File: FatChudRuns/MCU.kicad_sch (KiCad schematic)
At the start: 16 parts, among them SW1 SW_Push, SW2 SW_DIP_x01, U1 STM32F107RBTx

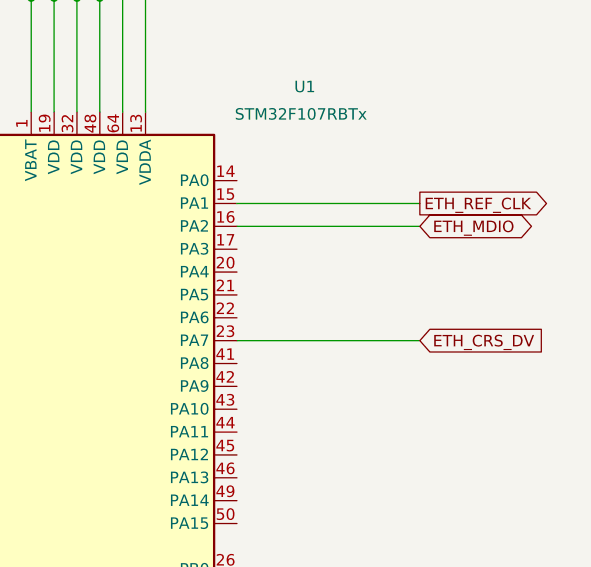
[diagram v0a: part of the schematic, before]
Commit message: connected phy to uC and added strapping options
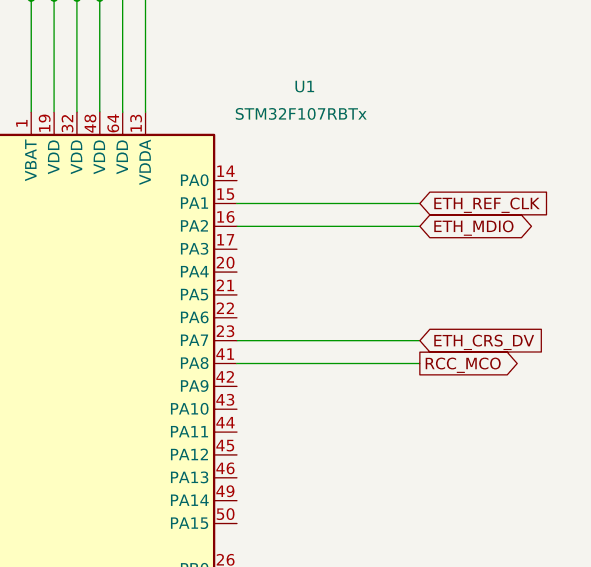
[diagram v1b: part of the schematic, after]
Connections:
- net RCC_MCO: now reaches U1.41 (PA8)
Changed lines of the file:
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@@
 	(generator "eeschema")
 	(generator_version "9.0")
-	(paper "A4")
+	(paper "A3")
 	(junction
 		(at 78.74 63.5)
@@
 		(pts
 			(xy 24.13 179.07) (xy 24.13 185.42)
+		)
+		(stroke
+			(width 0)
+			(type default)
+		)
+	)
+	(wire
+		(pts
+			(xy 170.18 78.74) (xy 190.5 78.74)
 		)
 		(stroke
@@
 		)
 	)
+	(global_label "RCC_MCO"
+		(shape output)
+		(at 190.5 78.74 0)
+		(fields_autoplaced yes)
+		(effects
+			(font
+				(size 1.27 1.27)
+			)
+			(justify left)
+		)
+		(property "Intersheetrefs" "${INTERSHEET_REFS}"
+			(at 202.4098 78.74 0)
+			(effects
+				(font
+					(size 1.27 1.27)
+				)
+				(justify left)
+				(hide yes)
+			)
+		)
+	)
 	(global_label "ETH_TXD0"
 		(shape output)
@@
 	)
 	(global_label "ETH_REF_CLK"
-		(shape output)
+		(shape input)
 		(at 190.5 60.96 0)
 		(fields_autoplaced yes)

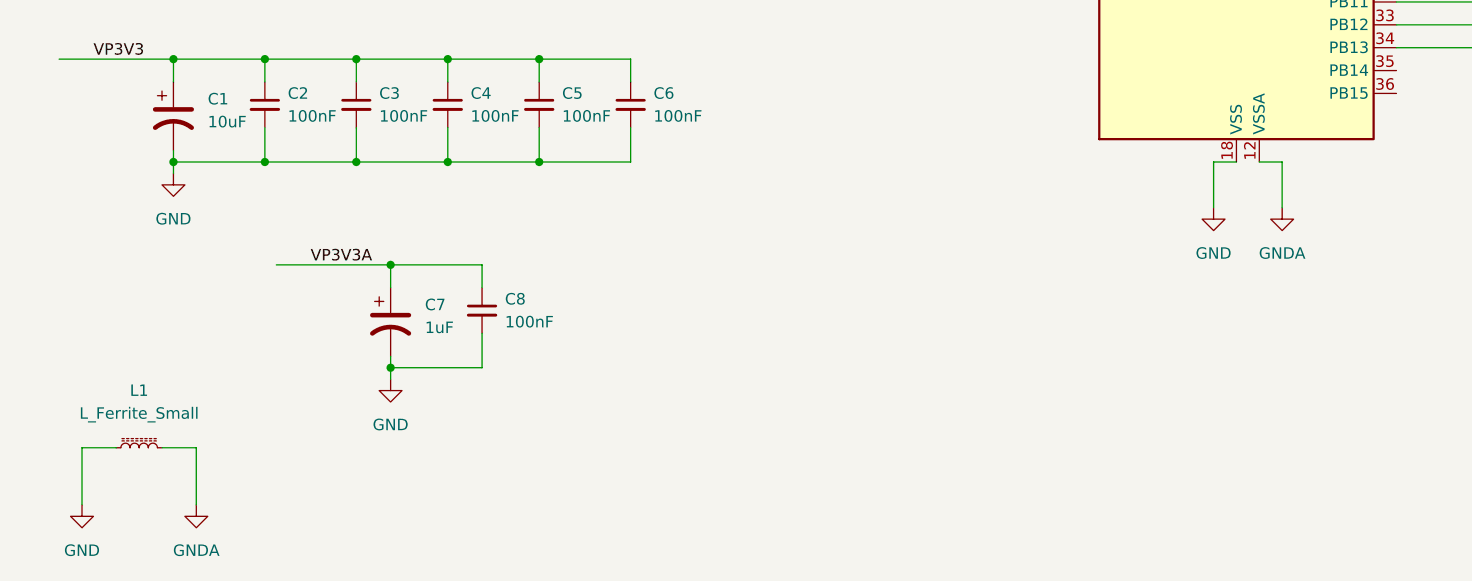
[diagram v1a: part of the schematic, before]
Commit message: selected rj45 w/ mag, fixed filtering for power, added snippets of layout recs
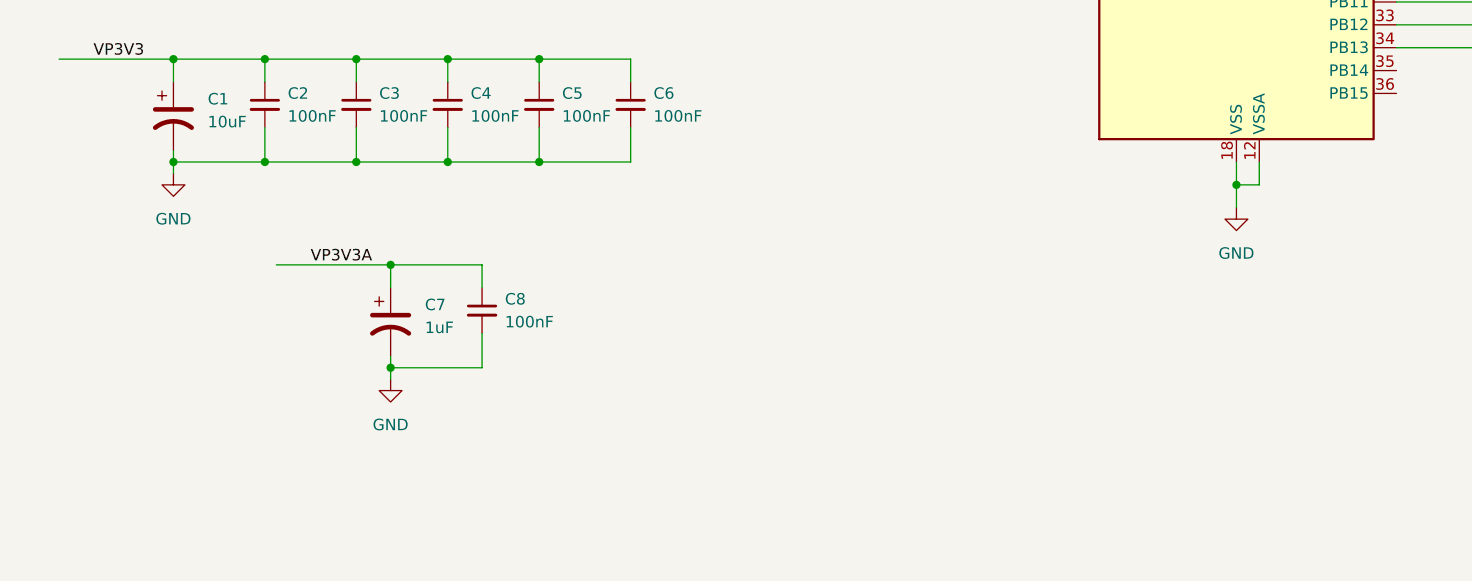
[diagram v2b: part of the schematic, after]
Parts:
- removed L1: L_Ferrite_Small, symbol Device:L_Ferrite_Small
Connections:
- net GNDA is gone; now on net GND: U1.12 (VSSA)

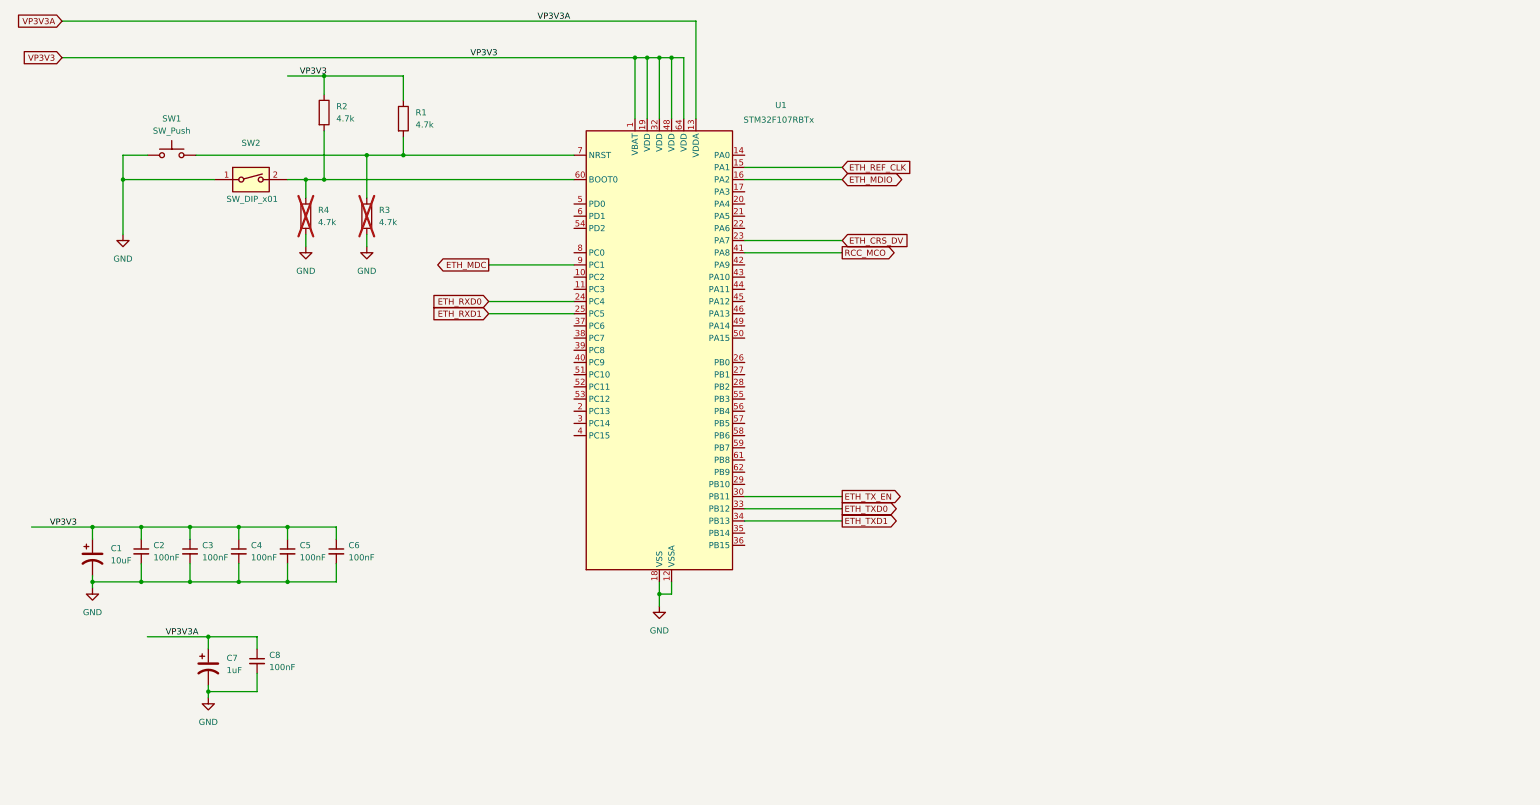
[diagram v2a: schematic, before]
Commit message: added connectors for gpio and jtag, need to verify orientation
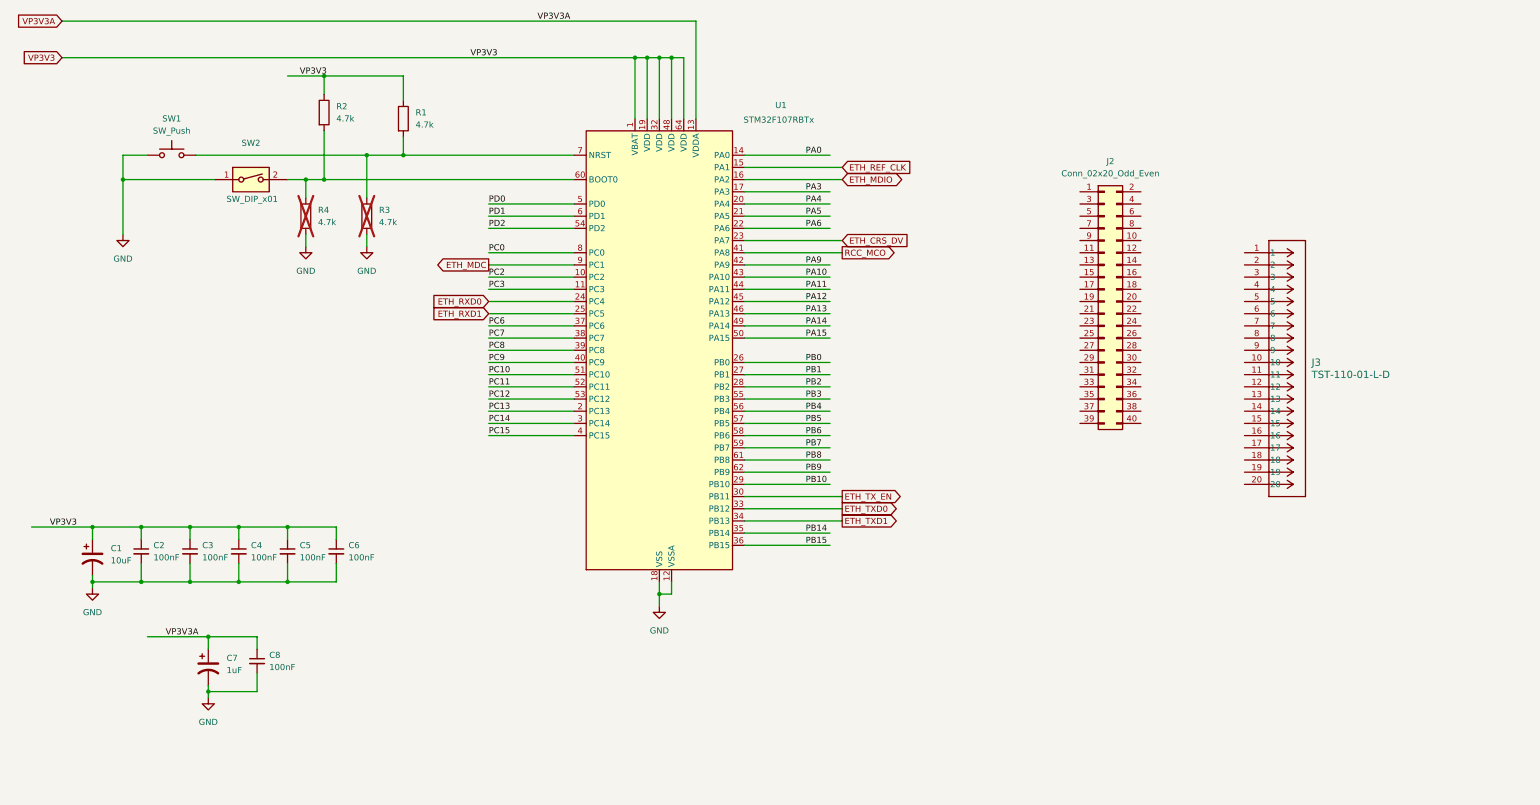
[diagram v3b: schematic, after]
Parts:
- added J2: Conn_02x20_Odd_Even, Connector_PinSocket_2.54mm:PinSocket_2x20_P2.54mm_Vertical, symbol Connector_Generic:Conn_02x20_Odd_Even
- added J3: TST-110-01-L-D, JTAG_20p_2.54mm:CONN20_TST_33P02X9P27_SAI, symbol TST_110_01_L_D:TST-110-01-L-D
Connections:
- net PC2: now reaches U1.10 (PC2)
- net PC3: now reaches U1.11 (PC3)
- net PA0: now reaches U1.14 (PA0)
- net PA3: now reaches U1.17 (PA3)
- net PC13: now reaches U1.2 (PC13)
- net PA4: now reaches U1.20 (PA4)
- net PA5: now reaches U1.21 (PA5)
- net PA6: now reaches U1.22 (PA6)
- net PB0: now reaches U1.26 (PB0)
- net PB1: now reaches U1.27 (PB1)
- net PB2: now reaches U1.28 (PB2)
- net PB10: now reaches U1.29 (PB10)
- net PC14: now reaches U1.3 (PC14)
- net PB14: now reaches U1.35 (PB14)
- net PB15: now reaches U1.36 (PB15)
- net PC6: now reaches U1.37 (PC6)
- net PC7: now reaches U1.38 (PC7)
- net PC8: now reaches U1.39 (PC8)
- net PC15: now reaches U1.4 (PC15)
- net PC9: now reaches U1.40 (PC9)
- net PA9: now reaches U1.42 (PA9)
- net PA10: now reaches U1.43 (PA10)
- net PA11: now reaches U1.44 (PA11)
- net PA12: now reaches U1.45 (PA12)
- net PA13: now reaches U1.46 (PA13)
- net PA14: now reaches U1.49 (PA14)
- net PD0: now reaches U1.5 (PD0)
- net PA15: now reaches U1.50 (PA15)
- net PC10: now reaches U1.51 (PC10)
- net PC11: now reaches U1.52 (PC11)
- net PC12: now reaches U1.53 (PC12)
- net PD2: now reaches U1.54 (PD2)
- net PB3: now reaches U1.55 (PB3)
- net PB4: now reaches U1.56 (PB4)
- net PB5: now reaches U1.57 (PB5)
- net PB6: now reaches U1.58 (PB6)
- net PB7: now reaches U1.59 (PB7)
- net PD1: now reaches U1.6 (PD1)
- net PB8: now reaches U1.61 (PB8)
- net PB9: now reaches U1.62 (PB9)
- net PC0: now reaches U1.8 (PC0)

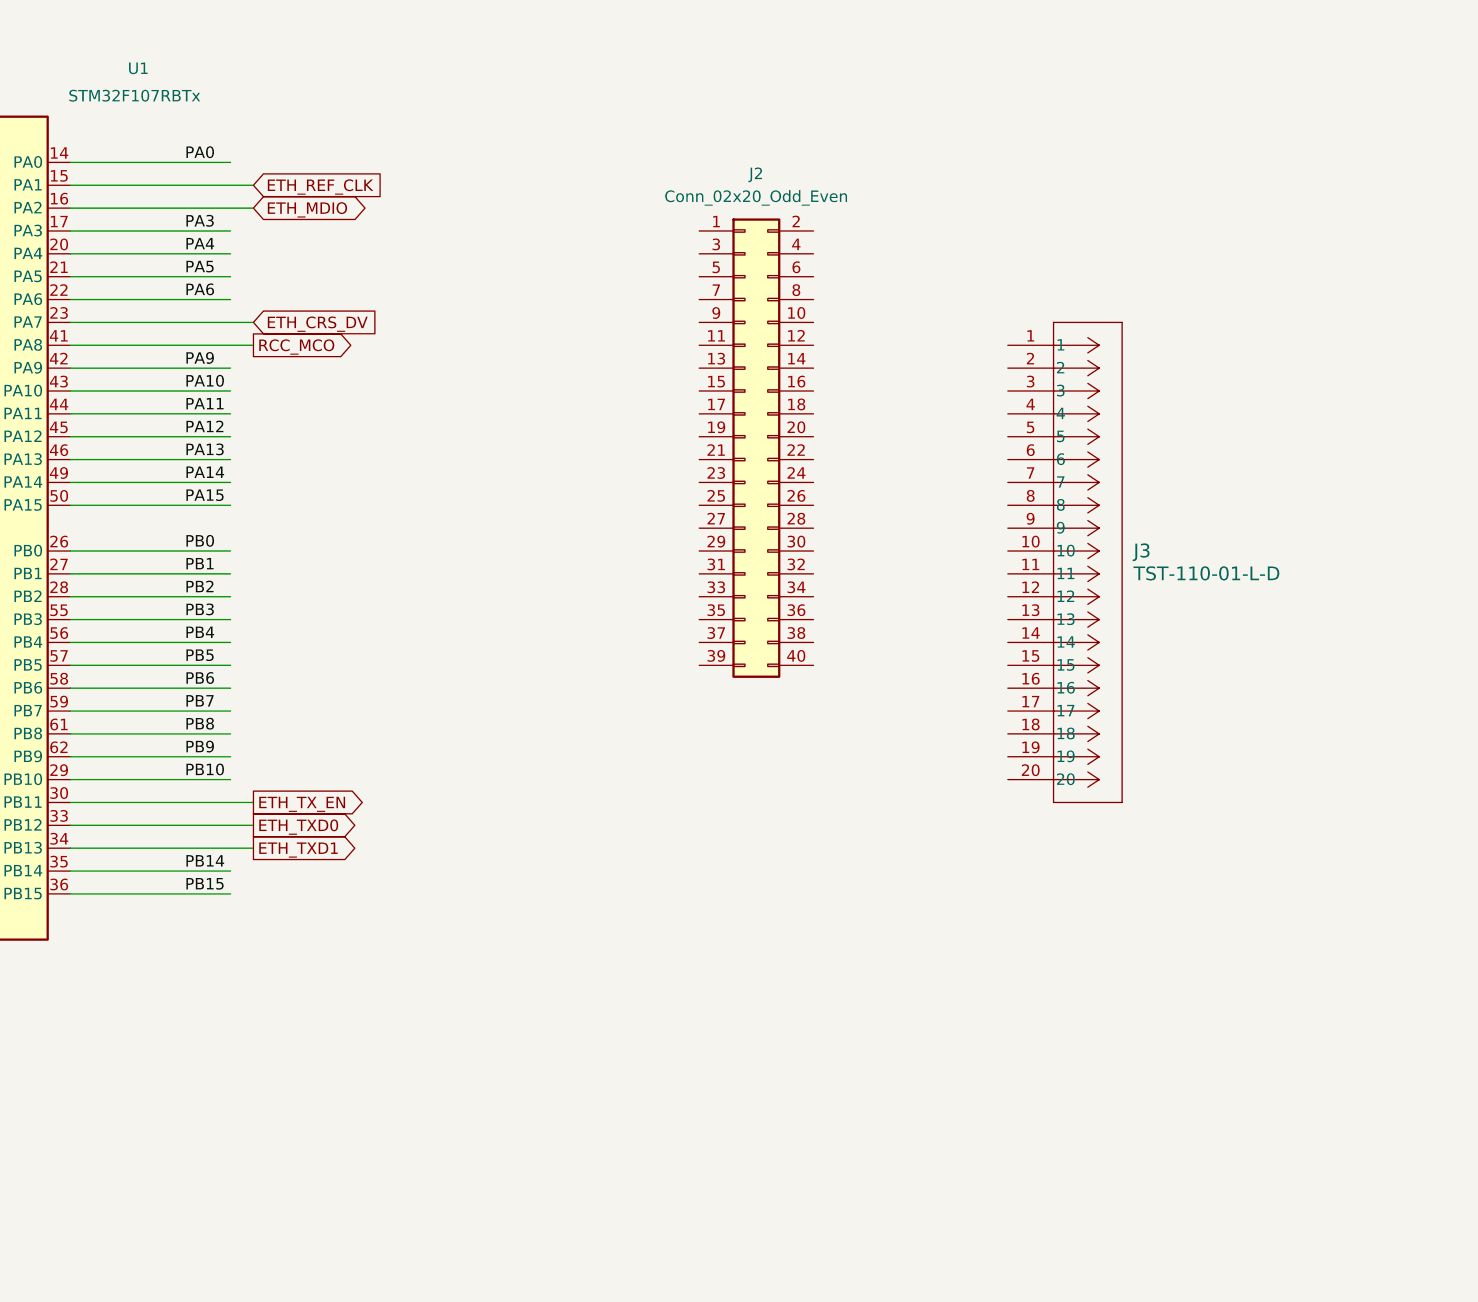
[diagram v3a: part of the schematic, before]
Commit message: added debugger and nucleo ref sch
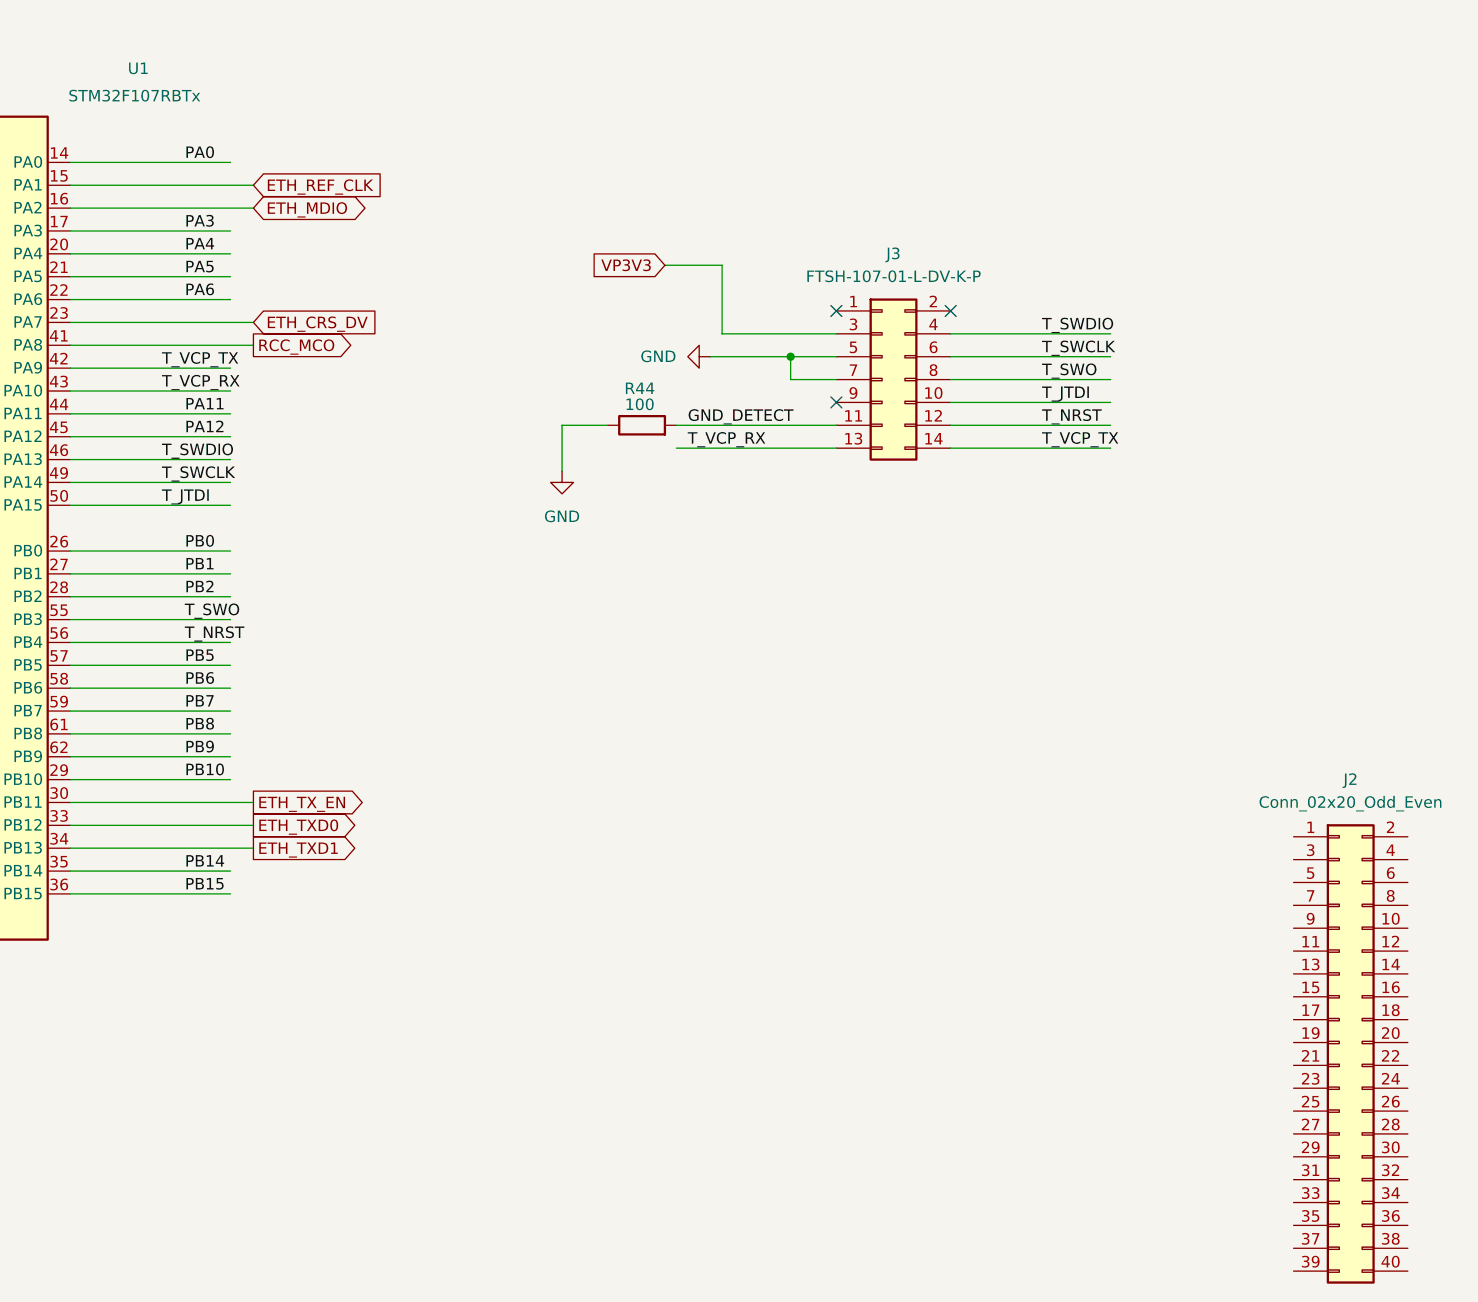
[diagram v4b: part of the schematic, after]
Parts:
- removed J3: TST-110-01-L-D, JTAG_20p_2.54mm:CONN20_TST_33P02X9P27_SAI, symbol TST_110_01_L_D:TST-110-01-L-D
- added J3: FTSH-107-01-L-DV-K-P, CON14_2X7_DUK_FTSH_SAI:CON14_2X7_DUK_FTSH_SAI, symbol Connector_Generic:Conn_02x07_Odd_Even
- added R44: 100, Resistor_SMD:R_0603_1608Metric, symbol Device:R
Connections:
- net GND: now also J3.5 (Pin_5), J3.7 (Pin_7), R44.1
- net VP3V3: now also J3.3 (Pin_3)
- net PA10 renamed T_VCP_RX
- net T_VCP_RX: now also J3.13 (Pin_13)
- net PA13 renamed T_SWDIO
- net T_SWDIO: now also J3.4 (Pin_4)
- net PA14 renamed T_SWCLK
- net T_SWCLK: now also J3.6 (Pin_6)
- net PA15 renamed T_JTDI
- net T_JTDI: now also J3.10 (Pin_10)
- net PA9 renamed T_VCP_TX
- net T_VCP_TX: now also J3.14 (Pin_14)
- net PB3 renamed T_SWO
- net T_SWO: now also J3.8 (Pin_8)
- net PB4 renamed T_NRST
- net T_NRST: now also J3.12 (Pin_12)
- new net GND_DETECT: J3.11 (Pin_11), R44.2
- no-connect marks 0 -> 3
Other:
- moved on the sheet: J2
